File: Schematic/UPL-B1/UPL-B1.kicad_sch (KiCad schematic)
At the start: 0 parts

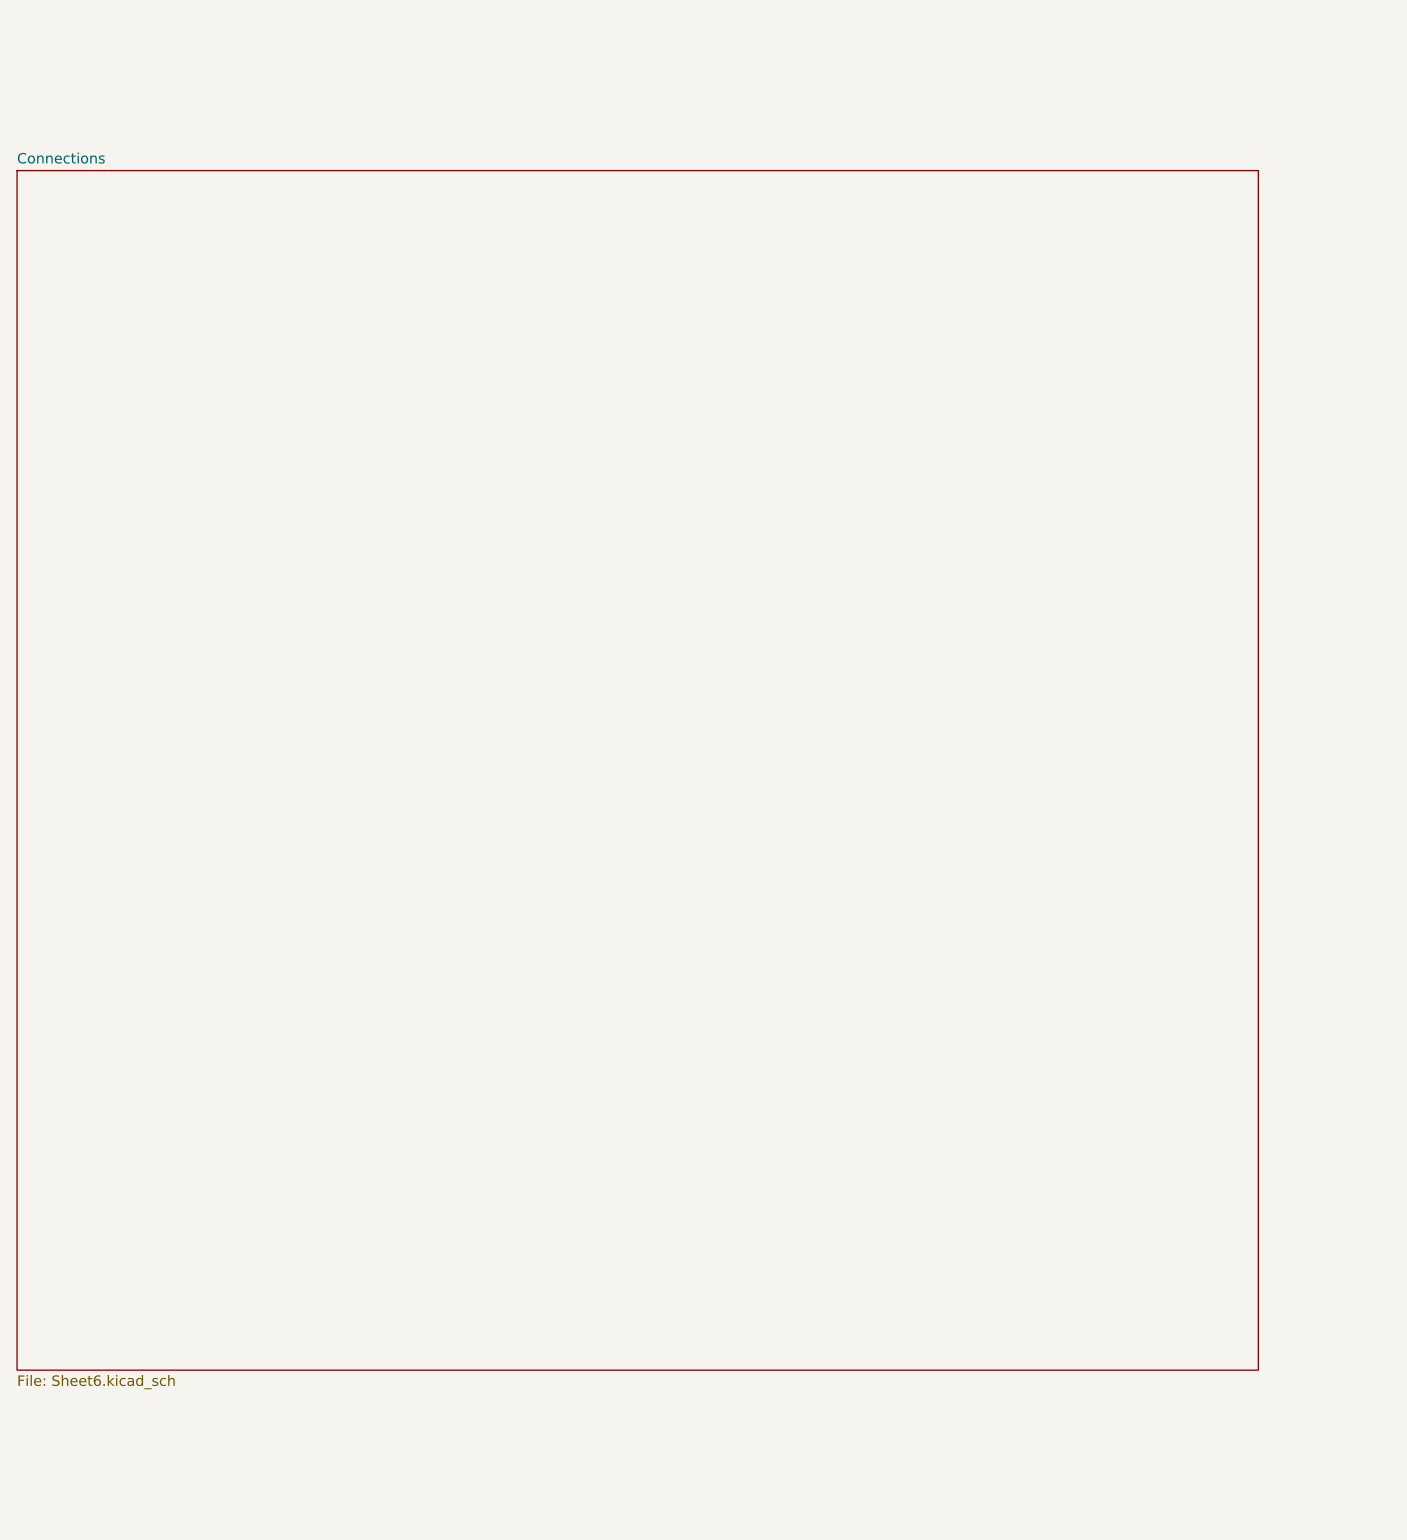
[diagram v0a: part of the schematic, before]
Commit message: Merge bvksound's changes to connector page
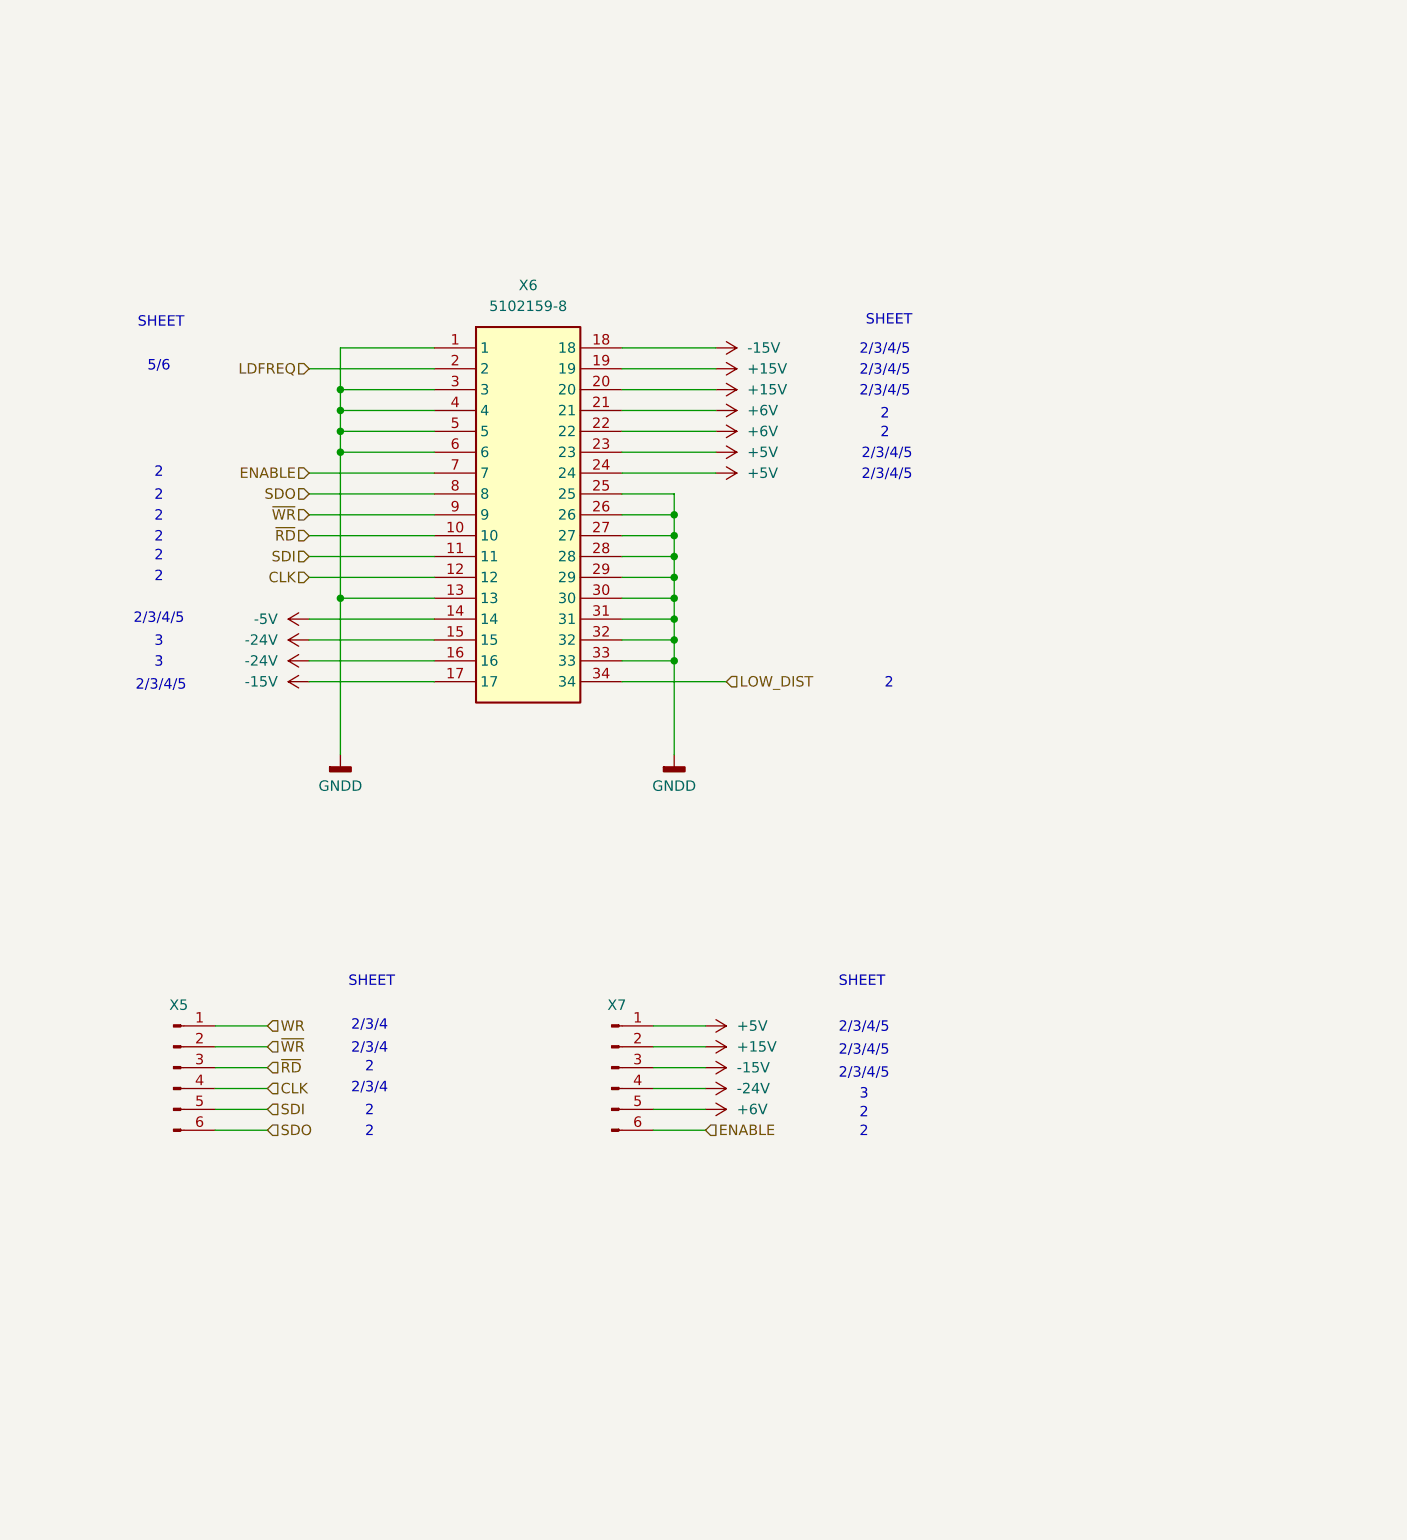
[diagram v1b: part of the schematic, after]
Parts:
- added X5, X7: Conn_01x06_Pin, symbol Connector:Conn_01x06_Pin
- added X6: 5102159-8, TYCO_5102159-8, symbol UPL_B1:5102159-8
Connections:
- net CLK: now also X5.4 (Pin_4), X6.12
- net ENABLE: now also X6.7, X7.6 (Pin_6)
- net WR: now also X5.1 (Pin_1)
- net ~{RD}: now also X5.3 (Pin_3), X6.10
- net ~{WR}: now also X5.2 (Pin_2), X6.9
- new net +15V: X6.19, X6.20, X7.2 (Pin_2)
- new net +5V: X6.23, X6.24, X7.1 (Pin_1)
- new net +6V: X6.21, X6.22, X7.5 (Pin_5)
- new net -15V: X6.17, X6.18, X7.3 (Pin_3)
- new net -24V: X6.15, X6.16, X7.4 (Pin_4)
- new net -5V: X6.14
- new net GNDD: X6.1, X6.13, X6.25, X6.26, X6.27, X6.28, X6.29, X6.3, X6.30, X6.31, X6.32, X6.33, X6.4, X6.5, X6.6
- new net LDFREQ: X6.2
- new net LOW_DIST: X6.34
- new net SDI: X5.5 (Pin_5), X6.11
- new net SDO: X5.6 (Pin_6), X6.8
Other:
- removed sheet Connections
- note added: "2"
- note added: "2/3/4"
- note added: "2/3/4/5"
- note added: "3"
- note added: "5/6"
- note added: "SHEET"

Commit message: added majority of footprints
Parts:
- X3: renamed from X5; footprint (none) -> Connector_PinHeader_2.54mm:PinHeader_1x06_P2.54mm_Vertical
- X4: renamed from X7; footprint (none) -> Connector_PinHeader_2.54mm:PinHeader_1x06_P2.54mm_Vertical
- renumbered X6 to X1
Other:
- note removed: "TODO -Digital Ground vs Analog ground? Today everything is using digital ground. ==> How was the B5 configured? -Finish hierarchical layout on Root page and double check all in and outputs -Start checking all components for availability"
- moved on the sheet: X1, X3, X4

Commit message: ERC fixes.
- Power flags added for power nets "hanging" off resistors.
- Add missing NC-markers for intentionally unconnected parts
- Fix -15V bridge between circuits on S4/S3
- Add +5 to /CLR of DAC
- Use non-hierachical labels on main sheet.
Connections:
- net CLK: no longer X1.12
- net ~{RD}: no longer X1.10
- net ~{WR}: no longer X1.9
- new net IN_CLK: X1.12
- new net /IN_RD: X1.10
- new net /IN_WR: X1.9
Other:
- sheet Integrator 1 & Loop Inverter ports: added none; removed ~{WR}

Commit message: renamed sheets and updated main connector
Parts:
- X1: footprint TYCO_5102159-8 -> UPL_B1:CONN_5103311-7_TYC
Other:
- sheet Integrator 1 & Loop Inverter: file Sheet3.kicad_sch -> Integrator 1 & Loop Inverter.kicad_sch
- sheet Integrator 2: file Sheet4.kicad_sch -> Integrator 2.kicad_sch
- sheet Level Control (ALC): file Sheet5.kicad_sch -> Level Control (ALC).kicad_sch
- sheet Output IMD Attenuator: file Sheet2.kicad_sch -> Output IMD Attenuator.kicad_sch
